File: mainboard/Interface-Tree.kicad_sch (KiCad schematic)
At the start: 0 parts

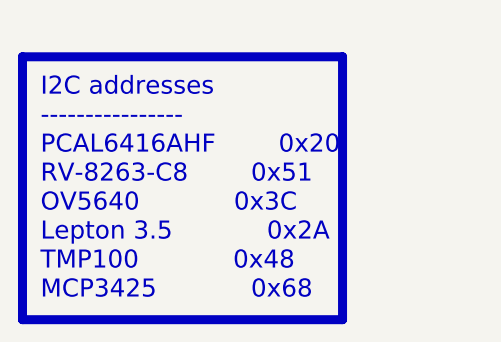
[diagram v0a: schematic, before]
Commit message: Continue routing, add flash LEDs for the RGB camera, add PWM controller for the Display Backlight and the flash LEDs, add Polyfuse for the battery
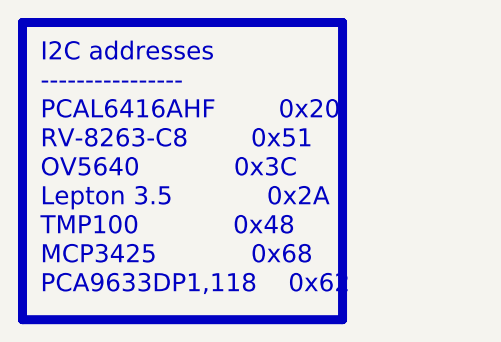
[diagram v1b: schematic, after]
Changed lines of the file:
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@@
 		(company "${COMPANY}")
 	)
-	(text_box "I2C addresses\n----------------\nPCAL6416AHF		0x20\nRV-8263-C8		0x51\nOV5640			0x3C\nLepton 3.5			0x2A\nTMP100			0x48\nMCP3425			0x68"
+	(text_box "I2C addresses\n----------------\nPCAL6416AHF		0x20\nRV-8263-C8		0x51\nOV5640			0x3C\nLepton 3.5			0x2A\nTMP100			0x48\nMCP3425			0x68\nPCA9633DP1,118	0x62"
 		(exclude_from_sim no)
-		(at 370.84 212.09 0)
-		(size 35.56 29.21)
+		(at 370.84 208.28 0)
+		(size 35.56 33.02)
 		(margins 2 2 2 2)
 		(stroke

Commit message: Remove ADC for battery measurement and add a fuel gauge
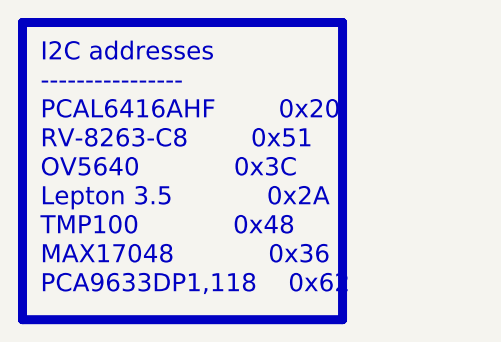
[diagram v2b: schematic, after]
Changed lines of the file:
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@@
 		(company "${COMPANY}")
 	)
-	(text_box "I2C addresses\n----------------\nPCAL6416AHF		0x20\nRV-8263-C8		0x51\nOV5640			0x3C\nLepton 3.5			0x2A\nTMP100			0x48\nMCP3425			0x68\nPCA9633DP1,118	0x62"
+	(text_box "I2C addresses\n----------------\nPCAL6416AHF		0x20\nRV-8263-C8		0x51\nOV5640			0x3C\nLepton 3.5			0x2A\nTMP100			0x48\nMAX17048			0x36\nPCA9633DP1,118	0x62"
 		(exclude_from_sim no)
 		(at 370.84 208.28 0)

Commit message: Layout complete
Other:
- title: Interface Tree -> Interface - Tree
